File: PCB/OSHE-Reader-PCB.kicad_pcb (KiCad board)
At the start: 2 copper layers, 8.7 x 4.4 mm, 27 parts, among them J1 USB_C_Receptacle_PowerOnly_24P, J2 112L-TDA0, J3 Conn_01x24_MountingPin, Q2 Si1308EDL, SW1 SW_Push, SW2 SW_Push, SW3 SW_Push, SW4 SW_Push, SW5 SW_Push, U1 BQ2057CSNTR, U2 IRF7326D2TRPBF, U3 TPS5432DDA

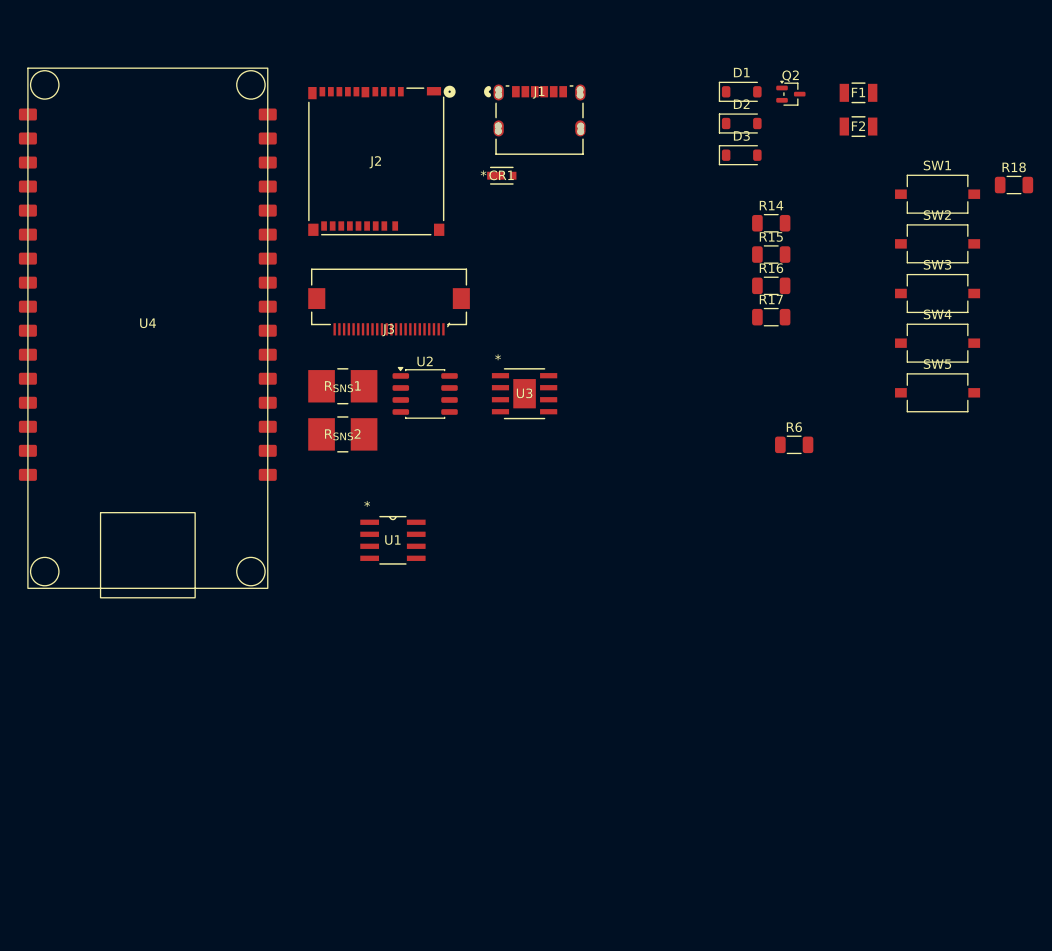
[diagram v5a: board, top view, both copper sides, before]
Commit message: Footprints added
All footprints added (problem with J1 for some reason) ((pads of the display driver))
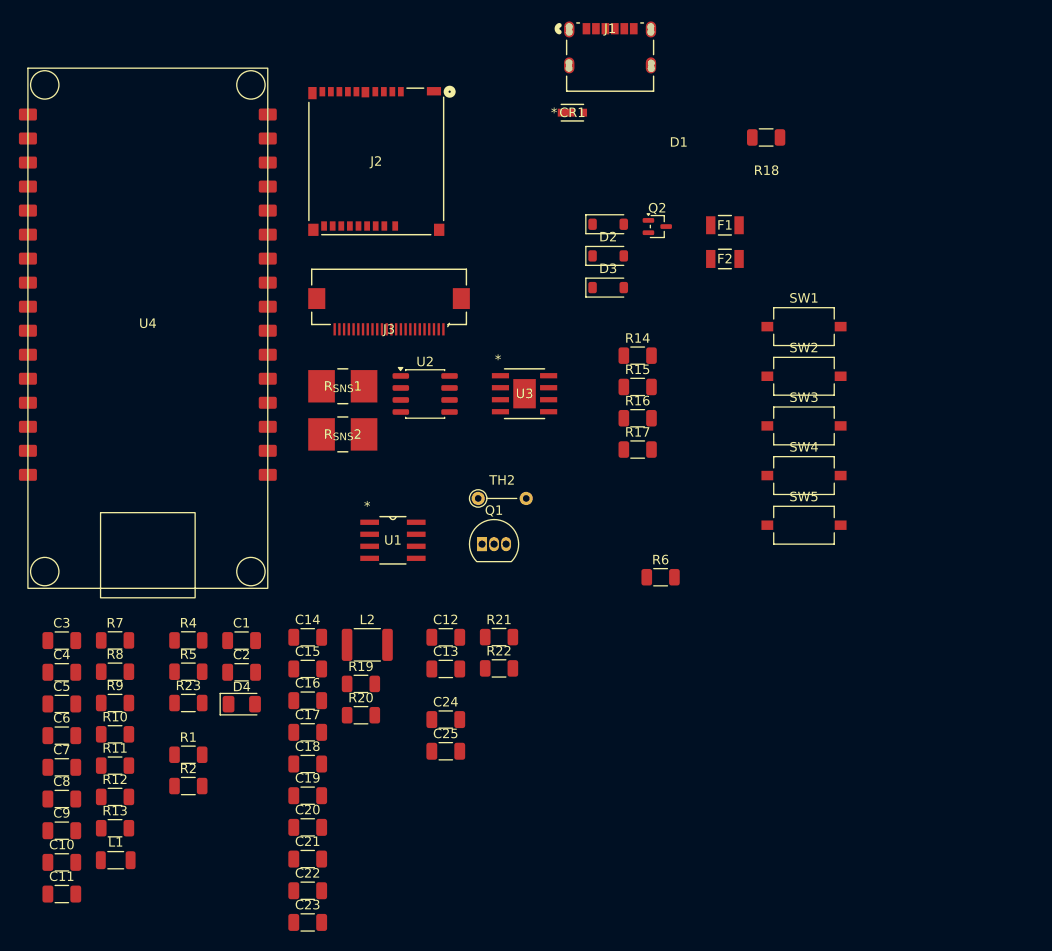
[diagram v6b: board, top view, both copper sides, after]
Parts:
- added C1: 0.1uF, Capacitor_SMD:C_1206_3216Metric, F.Cu at (48.0, 81.7)
- added C10: 22uF, Capacitor_SMD:C_1206_3216Metric, F.Cu at (29.0, 105.2)
- added C11: 22uF, Capacitor_SMD:C_1206_3216Metric, F.Cu at (29.0, 108.5)
- added C12: 0.1uF, Capacitor_SMD:C_1206_3216Metric, F.Cu at (69.6, 81.3)
- added C13: 10uF, Capacitor_SMD:C_1206_3216Metric, F.Cu at (69.6, 84.7)
- added C14: 4.7uF, Capacitor_SMD:C_1206_3216Metric, F.Cu at (55.0, 81.3)
- added C15: 10uF/50V, Capacitor_SMD:C_1206_3216Metric, F.Cu at (55.0, 84.7)
- added C16: 4.7uF/50V, Capacitor_SMD:C_1206_3216Metric, F.Cu at (55.0, 88.0)
- added C17: 1uF/50V, Capacitor_SMD:C_1206_3216Metric, F.Cu at (55.0, 91.4)
- added C18: 1uF/50V, Capacitor_SMD:C_1206_3216Metric, F.Cu at (55.0, 94.8)
- added C19: 1uF/50V, Capacitor_SMD:C_1206_3216Metric, F.Cu at (55.0, 98.1)
- added C2: 0.1uF, Capacitor_SMD:C_1206_3216Metric, F.Cu at (48.0, 85.0)
- added C20: 1uF/50V, Capacitor_SMD:C_1206_3216Metric, F.Cu at (55.0, 101.5)
- added C21: 1uF/50V, Capacitor_SMD:C_1206_3216Metric, F.Cu at (55.0, 104.8)
- added C22: 1uF/50V, Capacitor_SMD:C_1206_3216Metric, F.Cu at (55.0, 108.2)
- added C23: 1uF/50V, Capacitor_SMD:C_1206_3216Metric, F.Cu at (55.0, 111.5)
- added C24: 0.1uF, Capacitor_SMD:C_1206_3216Metric, F.Cu at (69.6, 90.0)
- added C25: 10uF, Capacitor_SMD:C_1206_3216Metric, F.Cu at (69.6, 93.4)
- added C3: 10uF, Capacitor_SMD:C_1206_3216Metric, F.Cu at (29.0, 81.7)
- added C4: 0.1uF, Capacitor_SMD:C_1206_3216Metric, F.Cu at (29.0, 85.0)
- added C5: 10nF, Capacitor_SMD:C_1206_3216Metric, F.Cu at (29.0, 88.4)
- added C6: 8.2nF, Capacitor_SMD:C_1206_3216Metric, F.Cu at (29.0, 91.8)
- added C7: 82pF, Capacitor_SMD:C_1206_3216Metric, F.Cu at (29.0, 95.1)
- added C8: 0.1uF, Capacitor_SMD:C_1206_3216Metric, F.Cu at (29.0, 98.5)
- added C9: 470pF, Capacitor_SMD:C_1206_3216Metric, F.Cu at (29.0, 101.8)
- added D4: LED, LED_SMD:LED_1206_3216Metric, F.Cu at (48.1, 88.4)
- added L1: 2.2uH, Inductor_SMD:L_1206_3216Metric, F.Cu at (34.7, 104.9)
- added L2: 10uH/1A, Inductor_SMD:L_1812_4532Metric, F.Cu at (61.3, 82.2)
- added Q1: PNP, Package_TO_SOT_THT:TO-92_Inline, F.Cu at (73.5, 71.5)
- added R1: 5.1K, Resistor_SMD:R_1206_3216Metric, F.Cu at (42.4, 93.8)
- added R10: 0, Resistor_SMD:R_1206_3216Metric, F.Cu at (34.7, 91.6)
- added R11: 49.9, Resistor_SMD:R_1206_3216Metric, F.Cu at (34.7, 94.9)
- added R12: 10k, Resistor_SMD:R_1206_3216Metric, F.Cu at (34.7, 98.2)
- added R13: 3.24k, Resistor_SMD:R_1206_3216Metric, F.Cu at (34.7, 101.5)
- added R19: 0.47R, Resistor_SMD:R_1206_3216Metric, F.Cu at (60.7, 86.3)
- added R2: 5.1K, Resistor_SMD:R_1206_3216Metric, F.Cu at (42.4, 97.1)
- added R20: 10K, Resistor_SMD:R_1206_3216Metric, F.Cu at (60.7, 89.6)
- added R21: 1M, Resistor_SMD:R_1206_3216Metric, F.Cu at (75.3, 81.3)
- added R22: 1M, Resistor_SMD:R_1206_3216Metric, F.Cu at (75.3, 84.6)
- added R23: 2k, Resistor_SMD:R_1206_3216Metric, F.Cu at (42.4, 88.3)
- added R4: R_{T1}/6.8K, Resistor_SMD:R_1206_3216Metric, F.Cu at (42.4, 81.7)
- added R5: 1k, Resistor_SMD:R_1206_3216Metric, F.Cu at (42.4, 85.0)
- added R7: 66.5, Resistor_SMD:R_1206_3216Metric, F.Cu at (34.7, 81.7)
- added R8: 45.3, Resistor_SMD:R_1206_3216Metric, F.Cu at (34.7, 85.0)
- added R9: 4.22k, Resistor_SMD:R_1206_3216Metric, F.Cu at (34.7, 88.3)
- added TH2: 10K, Resistor_THT:R_Axial_DIN0204_L3.6mm_D1.6mm_P5.08mm_Vertical, F.Cu at (73.0, 66.7)
- moved R18 26.7 mm to (103.5, 28.5)
- moved F2 19.9 mm to (99.1, 41.3)
- moved D1 19.9 mm to (86.8, 37.7)
- moved D2 19.9 mm to (86.8, 41.0)
- moved D3 19.9 mm to (86.8, 44.4)
- moved F1 19.9 mm to (99.1, 37.8)
- moved Q2 19.9 mm to (92.0, 37.9)
- moved R14 19.9 mm to (89.9, 51.6)
- moved R15 19.9 mm to (89.9, 54.9)
- moved R16 19.9 mm to (89.9, 58.2)
- moved R17 19.9 mm to (89.9, 61.5)
- moved R6 19.9 mm to (92.3, 75.0)
- moved SW1 19.9 mm to (107.5, 48.5)
- moved SW2 19.9 mm to (107.5, 53.8)
- moved SW3 19.9 mm to (107.5, 59.0)
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
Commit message: PCB Work
Fiddled with PCB :/
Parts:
- moved SW1 177.1 mm to (-49.5, 130.5)
- moved SW2 177.1 mm to (-49.5, 135.8)
- moved SW3 177.1 mm to (-49.5, 141.0)
- moved SW4 177.1 mm to (-49.5, 146.2)
- moved SW5 177.1 mm to (-49.5, 151.5)
- moved C10 116.6 mm to (-87.4, 110.2)
- moved C11 116.6 mm to (-87.4, 113.6)
- moved C12 116.6 mm to (-46.8, 86.4)
- moved C13 116.6 mm to (-46.8, 89.8)
- moved C14 116.6 mm to (-61.4, 86.4)
- moved C15 116.6 mm to (-61.4, 89.8)
- moved C16 116.6 mm to (-61.4, 93.1)
- moved C17 116.6 mm to (-61.4, 96.5)
- moved C18 116.6 mm to (-61.4, 99.8)
- moved C19 116.6 mm to (-61.4, 103.2)
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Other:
- copper layers 2 -> 4

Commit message: PCB
PCB
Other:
- board size 8.7 x 4.4 mm -> 118.5 x 160.4 mm
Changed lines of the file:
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@@
 		)
+	)
+	(gr_rect
+		(start 19 19)
+		(end 137.5 179.4)
+		(stroke
+			(width 0.05)
+			(type solid)
+		)
+		(fill no)
+		(layer "Edge.Cuts")
 	)
 	(embedded_fonts no)
